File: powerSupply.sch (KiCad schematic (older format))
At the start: 43 parts, among them U10 TPS7A4901, U11 LM3480, U12 TPS7A3001, U13 TPS7A3001, U14 LM3880, U8 TPS7A4901, U9 TPS7A4901

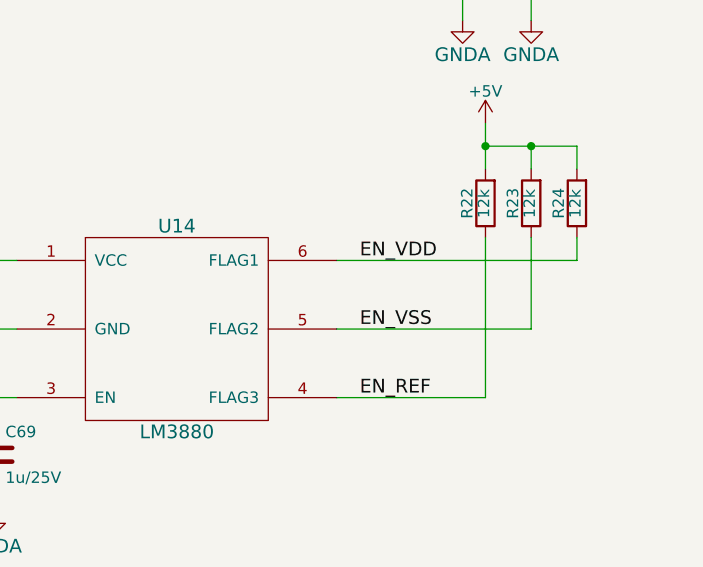
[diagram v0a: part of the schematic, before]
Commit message: Updated silkscreen to reflect version 2.2
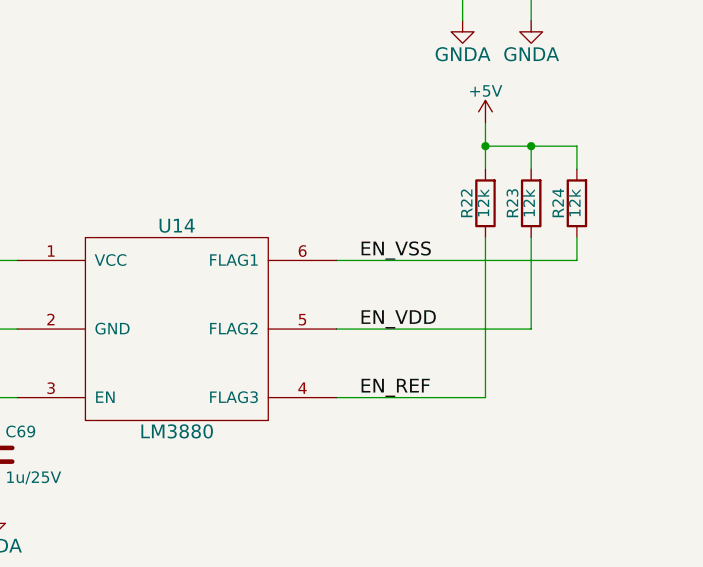
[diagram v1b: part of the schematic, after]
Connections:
- net EN_VDD: now also R23.1, U14.5 (FLAG2); no longer R24.1, U14.6 (FLAG1)
- net EN_VSS: now also R24.1, U14.6 (FLAG1); no longer R23.1, U14.5 (FLAG2)
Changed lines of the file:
@@
 	9400 5800 10050 5800
 Text Label 9500 5200 0    60   ~ 0
+EN_VSS
+Text Label 9500 5500 0    60   ~ 0
 EN_VDD
-Text Label 9500 5500 0    60   ~ 0
-EN_VSS
 Text Label 9500 5800 0    60   ~ 0
 EN_REF
